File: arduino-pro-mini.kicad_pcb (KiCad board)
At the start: 2 copper layers, 17.8 x 33 mm, 21 parts, among them Q1 Resonator, U1 ATMEGA328-A, U2 MIC5205

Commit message: update
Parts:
- added R1: R, Resistors_SMD:R_0603, B.Cu at (126.3, 94.4)
- added R3: R, Resistors_SMD:R_0603, B.Cu at (128.0, 94.4)
- SJ1: footprint Resistors_SMD:R_0603 -> arduino-pro-mini:jumper
- moved C1 2.20 mm to (118.3, 116.6)
- moved R2 1.95 mm to (119.8, 111.7), turned to 180 degrees
- moved Q1 0.68 mm to (118.6, 97.9)
- moved C13 0.60 mm to (119.2, 91.0)
- moved S1 0.57 mm to (123.5, 115.5)
- moved SJ1 0.55 mm to (119.1, 94.9), turned to 270 degrees
- moved C19 0.52 mm to (127.3, 93.3)
- moved R6 0.51 mm to (128.5, 114.3), turned to 90 degrees
- moved D3 0.46 mm to (128.5, 116.8)
- moved C3 0.23 mm to (122.9, 111.7)
- moved C10 0.22 mm to (121.5, 96.6)
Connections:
- JP1 pad 1: DTR -> GND
- JP1 pad 2: TXO -> GND
- JP1 pad 3: RXI -> VCC
- JP1 pad 4: VCC -> RXI
- JP1 pad 5: GND -> TXO
- JP1 pad 6: GND -> DTR
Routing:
- net RESET: track 0.00 -> 59.8 mm, vias 0 -> 2
- net VCC: track 0.00 -> 54.8 mm, vias 0 -> 2
- net RXI: track 0.00 -> 36.9 mm, vias 0 -> 1
- net TXO: track 0.00 -> 24.9 mm
- net D10: track 0.00 -> 24.0 mm, vias 0 -> 1
- net Net-(C1-Pad1): track 0.00 -> 21.3 mm, vias 0 -> 2
- net MISO: track 0.00 -> 15.7 mm, vias 0 -> 1
- net MOSI: track 0.00 -> 15.6 mm, vias 0 -> 1
- net A5: track 0.00 -> 15.3 mm, vias 0 -> 1
- net GND: track 0.00 -> 15.1 mm, vias 0 -> 3
- net RAW: track 0.00 -> 13.3 mm, vias 0 -> 2
- net D9: track 0.00 -> 11.8 mm
- net D4: track 0.00 -> 11.1 mm, vias 0 -> 1
- net SCK: track 0.00 -> 11.0 mm
- net D3: track 0.00 -> 10.8 mm, vias 0 -> 1
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- added copper zone on B.Cu, net GND
- added copper zone on F.Cu, net GND
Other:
- board size 17.8 x 33 mm -> 18 x 33.1 mm

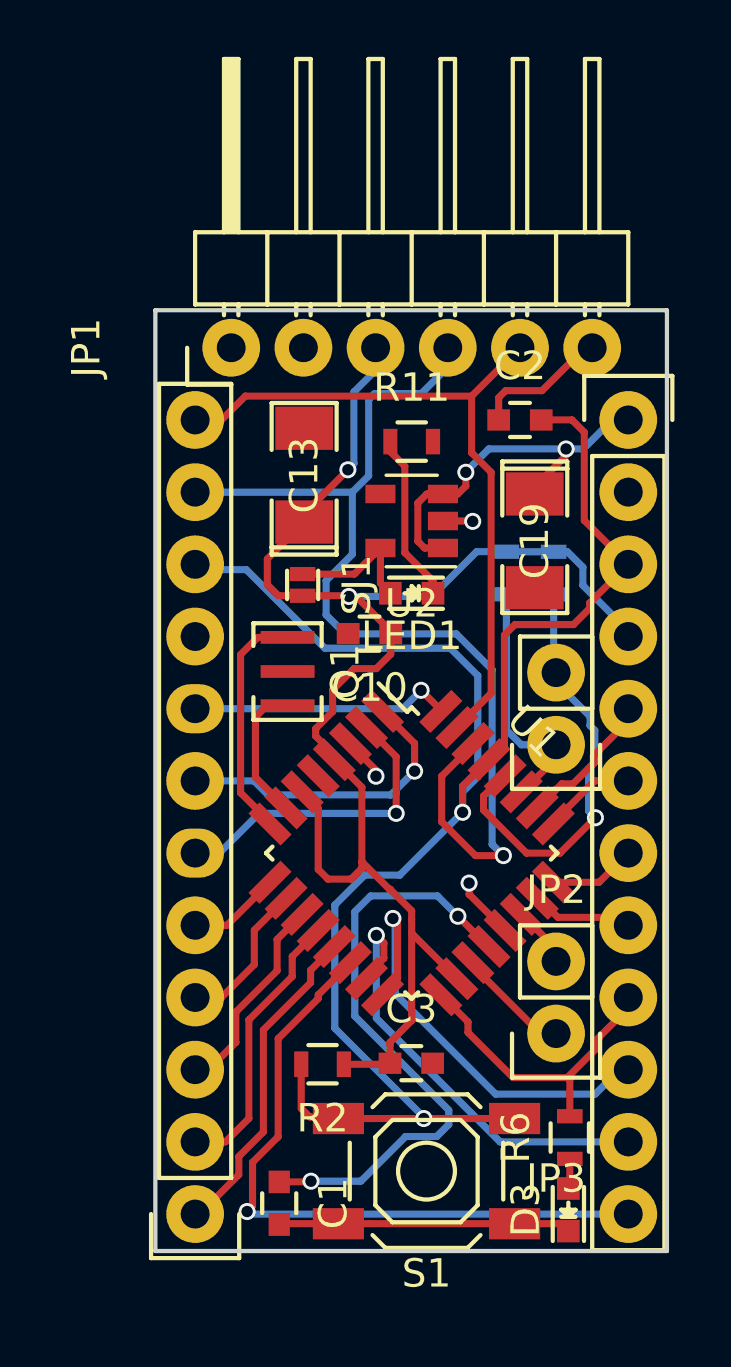
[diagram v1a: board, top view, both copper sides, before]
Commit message: added pin labels
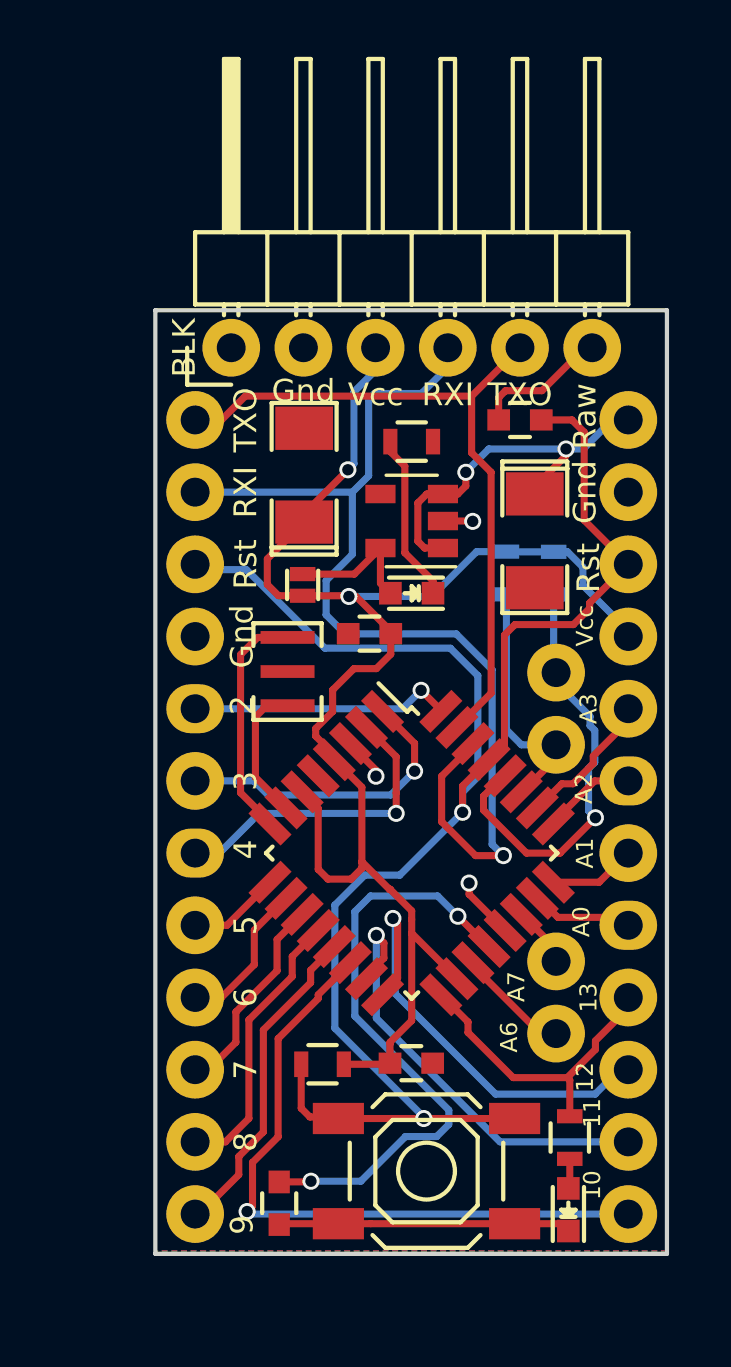
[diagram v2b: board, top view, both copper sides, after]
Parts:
- JP2, JP3: footprint Pin_Headers:Pin_Header_Straight_1x02 -> arduino-pro-mini:Pin_Header_Straight_1x02
- JP6, JP7: footprint Pin_Headers:Pin_Header_Straight_1x12 -> arduino-pro-mini:Pin_Header_Straight_1x12
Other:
- board size 18 x 33.1 mm -> 18 x 33.2 mm
- board text added: "10"
- board text added: "11"
- board text added: "12"
- board text added: "13"
- board text added: "2"
- board text added: "3"
- board text added: "4"
- board text added: "5"
- board text added: "6"
- board text added: "7"
- board text added: "8"
- board text added: "9"
- board text added: "A0"
- board text added: "A1"
- board text added: "A2"
- board text added: "A3"
- board text added: "A6"
- board text added: "A7"
- board text added: "BLK"
- board text added: "Gnd"
- board text added: "RXI"
- board text added: "Raw"
- board text added: "Rst"
- board text added: "TXO"
- board text added: "Vcc"
